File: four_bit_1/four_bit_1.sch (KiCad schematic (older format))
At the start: 1 part, among them P1 DIN_41612_128P

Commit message: Added erasable memory, and fixed lots of random wiring errors.
I decided to go with a 16-bit-wide MRAM chip -- I had  no idea
until I started researching RAM options how technologically
similar MRAM is to core memory. The datasheet diagrams look like
they're straight out of the AGC documentation!

There's a slight inaccuracy in this implementation worth mentioning.
Like fixed memory, I've wired the sense amplifier outputs directly up
to the tristate data output pins of the MRAM chip. But because the
data lines are bidirectional, data being written into RAM will show up
on the sense lines, and go straight into the ungated G register. Since
G is what's being written out, this doesn't matter 99% of the time, but
if there's an overflow condition in G (I don't even know if this is
possible), the bit 16 will be copied over bit 16, and the overflow
condition will be lost. I'll keep an eye out to see if anything relies
on G not changing after the write cycle is complete.

With erasable memory introduced, the computer now theoretically supports
all programs that don't use I/O or interrupts. I've started running
the VirtualAGC validation program, and have been fixing random errors
uncovered by failing self-tests.
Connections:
- net GND: no longer P1.93 (29C), P1.94 (30C), P1.95 (31C), P1.96 (32C)
- new net GEM01: P1.93 (29C)
- new net GEM02: P1.94 (30C)
- new net GEM03: P1.95 (31C)
- new net GEM04: P1.96 (32C)
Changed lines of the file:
@@
 Wire Wire Line
 	4300 8350 4200 8350
-$Comp
-L GND #PWR08
-U 1 1 56A4BF3C
-P 9850 4200
-F 0 "#PWR08" H 9850 3950 50  0001 C CNN
-F 1 "GND" H 9850 4050 50  0000 C CNN
-F 2 "" H 9850 4200 60  0000 C CNN
-F 3 "" H 9850 4200 60  0000 C CNN
-	1    9850 4200
-	1    0    0    -1
-$EndComp
-Wire Wire Line
-	9850 3750 9950 3750
-Wire Wire Line
-	9850 3850 9950 3850
-Connection ~ 9850 3850
-Wire Wire Line
-	9850 3950 9950 3950
-Connection ~ 9850 3950
-Wire Wire Line
-	9850 4050 9950 4050
-Connection ~ 9850 4050
 Wire Wire Line
 	5700 2000 6550 2000
@@
 Wire Wire Line
 	5700 3950 5800 3950
-Wire Wire Line
-	9850 3750 9850 4200
 Text GLabel 9850 2150 0    60   BiDi ~ 0
 RL01/
@@
 Wire Wire Line
 	9950 2450 9850 2450
+Text GLabel 3250 3600 2    60   Output ~ 0
+GEM01
+Wire Wire Line
+	3150 3600 3250 3600
+Text GLabel 3250 3700 2    60   Output ~ 0
+GEM02
+Wire Wire Line
+	3150 3700 3250 3700
+Text GLabel 5800 3600 2    60   Output ~ 0
+GEM03
+Wire Wire Line
+	5700 3600 5800 3600
+Text GLabel 5800 3700 2    60   Output ~ 0
+GEM04
+Wire Wire Line
+	5700 3700 5800 3700
+Text GLabel 9850 3750 0    60   Input ~ 0
+GEM01
+Wire Wire Line
+	9950 3750 9850 3750
+Text GLabel 9850 3850 0    60   Input ~ 0
+GEM02
+Wire Wire Line
+	9950 3850 9850 3850
+Text GLabel 9850 3950 0    60   Input ~ 0
+GEM03
+Wire Wire Line
+	9950 3950 9850 3950
+Text GLabel 9850 4050 0    60   Input ~ 0
+GEM04
+Wire Wire Line
+	9950 4050 9850 4050
 $EndSCHEMATC

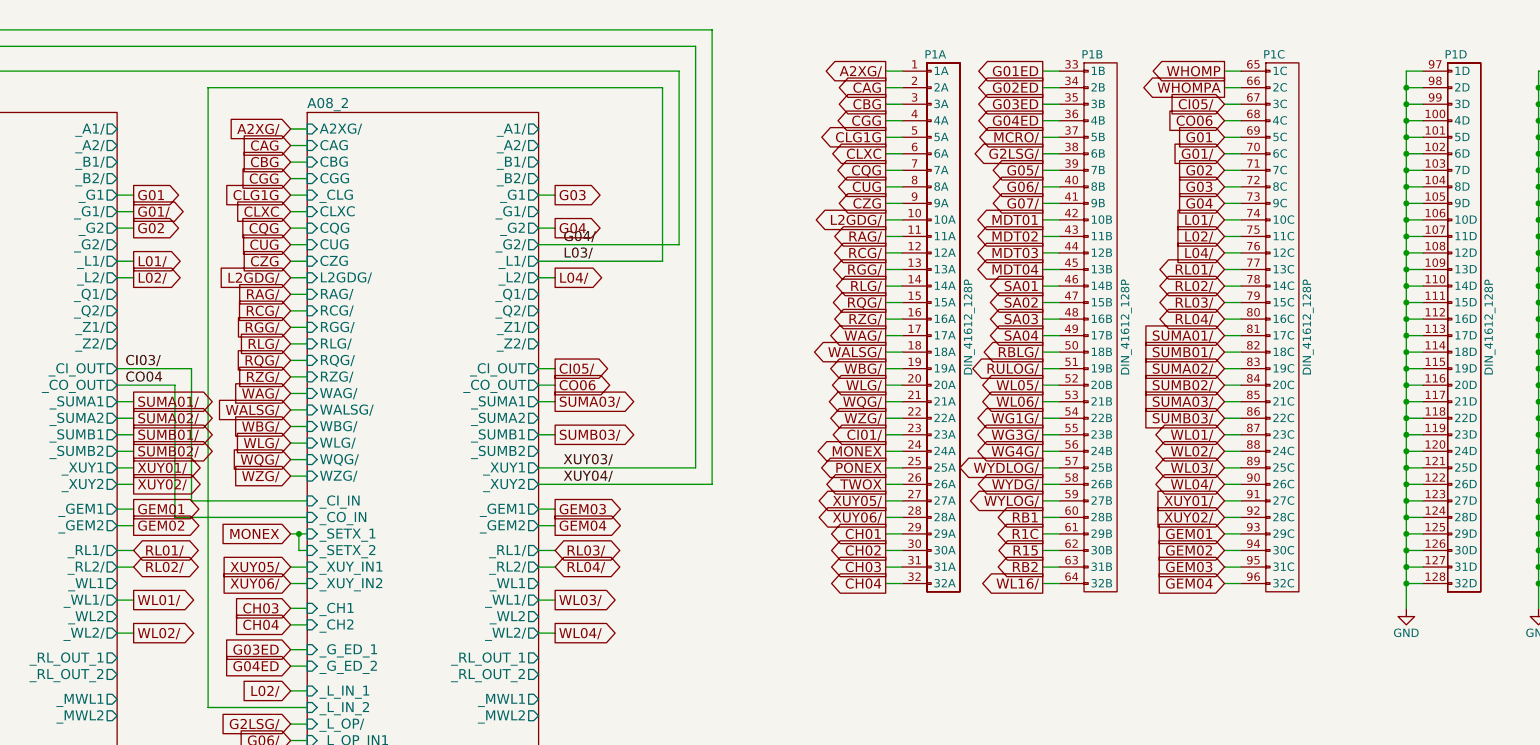
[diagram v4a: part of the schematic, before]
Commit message: Added and tied in Inout VII, the final logic module!
I still need to comb through the schematics to see if there are any
stray gates I missed. The initial conditions are also pretty much
guaranteed to be wrong. But it's mostly all there!
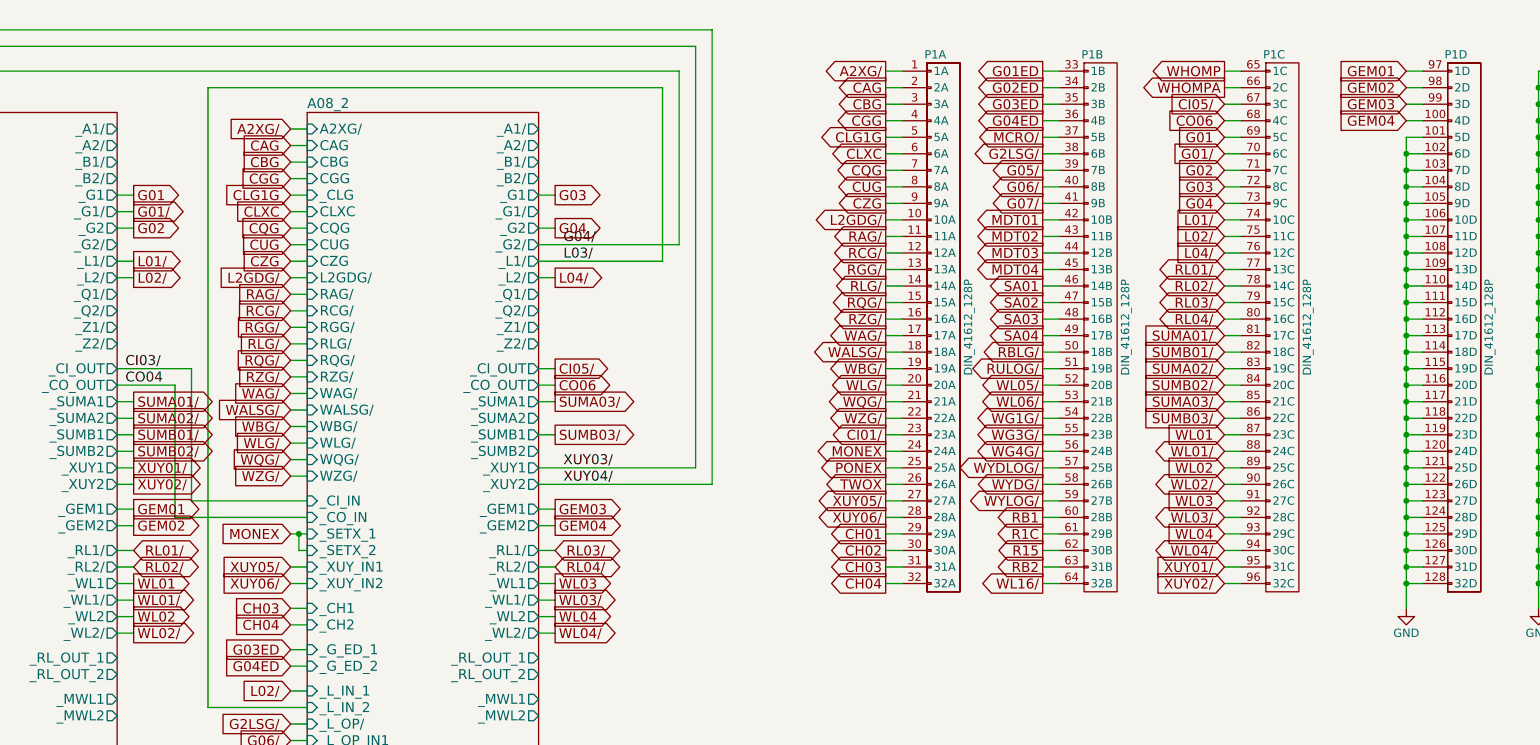
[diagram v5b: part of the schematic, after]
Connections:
- net GEM01: now also P1.97 (1D); no longer P1.93 (29C)
- net GEM02: now also P1.98 (2D); no longer P1.94 (30C)
- net GEM03: now also P1.99 (3D); no longer P1.95 (31C)
- net GEM04: now also P1.100 (4D); no longer P1.96 (32C)
- net GND: no longer P1.100 (4D), P1.97 (1D), P1.98 (2D), P1.99 (3D)
- net WL01/: now also P1.88 (24C); no longer P1.87 (23C)
- net WL02/: now also P1.90 (26C); no longer P1.88 (24C)
- net WL03/: now also P1.92 (28C); no longer P1.89 (25C)
- net WL04/: now also P1.94 (30C); no longer P1.90 (26C)
- net XUY01/: now also P1.95 (31C); no longer P1.91 (27C)
- net XUY02/: now also P1.96 (32C); no longer P1.92 (28C)
- new net WL01: P1.87 (23C)
- new net WL02: P1.89 (25C)
- new net WL03: P1.91 (27C)
- new net WL04: P1.93 (29C)
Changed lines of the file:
@@
 L02/
 Wire Wire Line
-	11050 950  10950 950
-Wire Wire Line
-	11050 1050 10950 1050
-Connection ~ 10950 1050
-Wire Wire Line
-	10950 1150 11050 1150
-Connection ~ 10950 1150
-Wire Wire Line
-	10950 1250 11050 1250
-Connection ~ 10950 1250
-Wire Wire Line
 	10950 1350 11050 1350
-Connection ~ 10950 1350
 Wire Wire Line
 	10950 1450 11050 1450
@@
 	10950 4050 11050 4050
 Connection ~ 10950 4050
-Wire Wire Line
-	10950 950  10950 4200
 Wire Wire Line
 	11850 950  11750 950
@@
 Wire Wire Line
 	9950 1950 9850 1950
-Text GLabel 9850 3150 0    60   BiDi ~ 0
+Text GLabel 9850 3250 0    60   BiDi ~ 0
 WL01/
 Wire Wire Line
-	9950 3150 9850 3150
-Text GLabel 9850 3250 0    60   BiDi ~ 0
+	9950 3250 9850 3250
+Text GLabel 9850 3450 0    60   BiDi ~ 0
 WL02/
 Wire Wire Line
-	9950 3250 9850 3250
-Text GLabel 9850 3350 0    60   BiDi ~ 0
+	9950 3450 9850 3450
+Text GLabel 9850 3650 0    60   BiDi ~ 0
 WL03/
 Wire Wire Line
-	9950 3350 9850 3350
-Text GLabel 9850 3450 0    60   BiDi ~ 0
+	9950 3650 9850 3650
+Text GLabel 9850 3850 0    60   BiDi ~ 0
 WL04/
 Wire Wire Line
-	9950 3450 9850 3450
+	9950 3850 9850 3850
 Text GLabel 5800 2750 2    60   Output ~ 0
 CI05/
@@
 Wire Wire Line
 	3150 3450 3250 3450
-Text GLabel 9850 3550 0    60   Input ~ 0
+Text GLabel 9850 3950 0    60   Input ~ 0
 XUY01/
 Wire Wire Line
-	9950 3550 9850 3550
-Text GLabel 9850 3650 0    60   Input ~ 0
+	9950 3950 9850 3950
+Text GLabel 9850 4050 0    60   Input ~ 0
 XUY02/
 Wire Wire Line
-	9950 3650 9850 3650
+	9950 4050 9850 4050
 Text GLabel 1650 8700 0    60   Input ~ 0
 WHOMPA
@@
 Wire Wire Line
 	5700 3700 5800 3700
+Text GLabel 10950 950  0    60   Input ~ 0
+GEM01
+Wire Wire Line
+	11050 950  10950 950
+Text GLabel 10950 1050 0    60   Input ~ 0
+GEM02
+Wire Wire Line
+	11050 1050 10950 1050
+Text GLabel 10950 1150 0    60   Input ~ 0
+GEM03
+Wire Wire Line
+	11050 1150 10950 1150
+Text GLabel 10950 1250 0    60   Input ~ 0
+GEM04
+Wire Wire Line
+	11050 1250 10950 1250
+Text GLabel 3250 4050 2    60   Output ~ 0
+WL01
+Wire Wire Line
+	3150 4050 3250 4050
+Text GLabel 3250 4250 2    60   Output ~ 0
+WL02
+Wire Wire Line
+	3150 4250 3250 4250
+Text GLabel 5800 4050 2    60   Output ~ 0
+WL03
+Wire Wire Line
+	5700 4050 5800 4050
+Text GLabel 5800 4250 2    60   Output ~ 0
+WL04
+Wire Wire Line
+	5700 4250 5800 4250
+Wire Wire Line
+	10950 1350 10950 4200
+Text GLabel 9850 3150 0    60   Input ~ 0
+WL01
+Wire Wire Line
+	9950 3150 9850 3150
+Text GLabel 9850 3350 0    60   Input ~ 0
+WL02
+Wire Wire Line
+	9950 3350 9850 3350
+Text GLabel 9850 3550 0    60   Input ~ 0
+WL03
+Wire Wire Line
+	9950 3550 9850 3550
 Text GLabel 9850 3750 0    60   Input ~ 0
-GEM01
+WL04
 Wire Wire Line
 	9950 3750 9850 3750
-Text GLabel 9850 3850 0    60   Input ~ 0
-GEM02
-Wire Wire Line
-	9950 3850 9850 3850
-Text GLabel 9850 3950 0    60   Input ~ 0
-GEM03
-Wire Wire Line
-	9950 3950 9850 3950
-Text GLabel 9850 4050 0    60   Input ~ 0
-GEM04
-Wire Wire Line
-	9950 4050 9850 4050
 $EndSCHEMATC

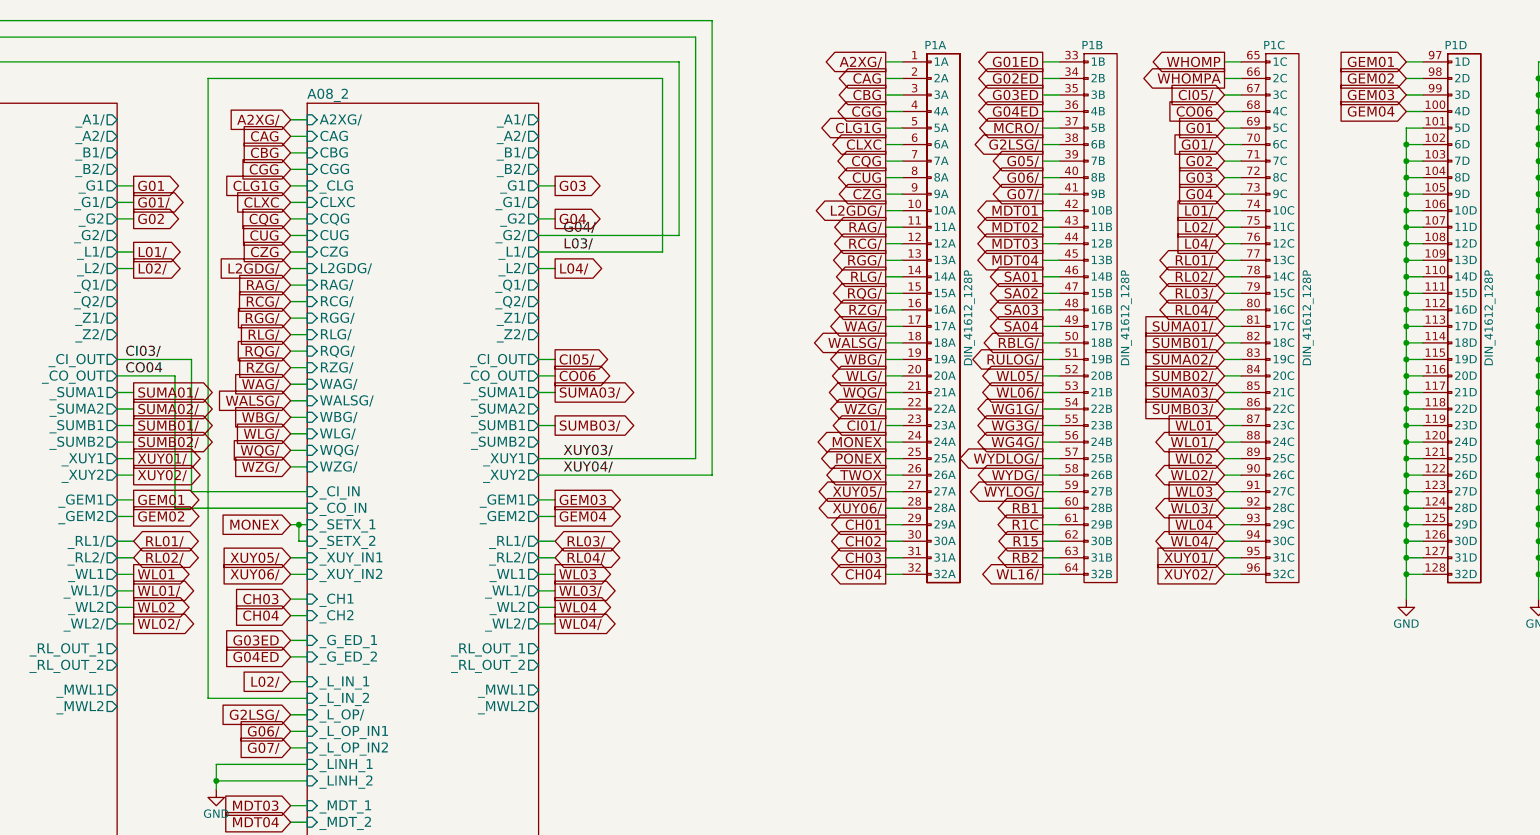
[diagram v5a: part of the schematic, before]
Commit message: Broke all the monitor outputs I could find out to the backplane, in preparation for making a monitor
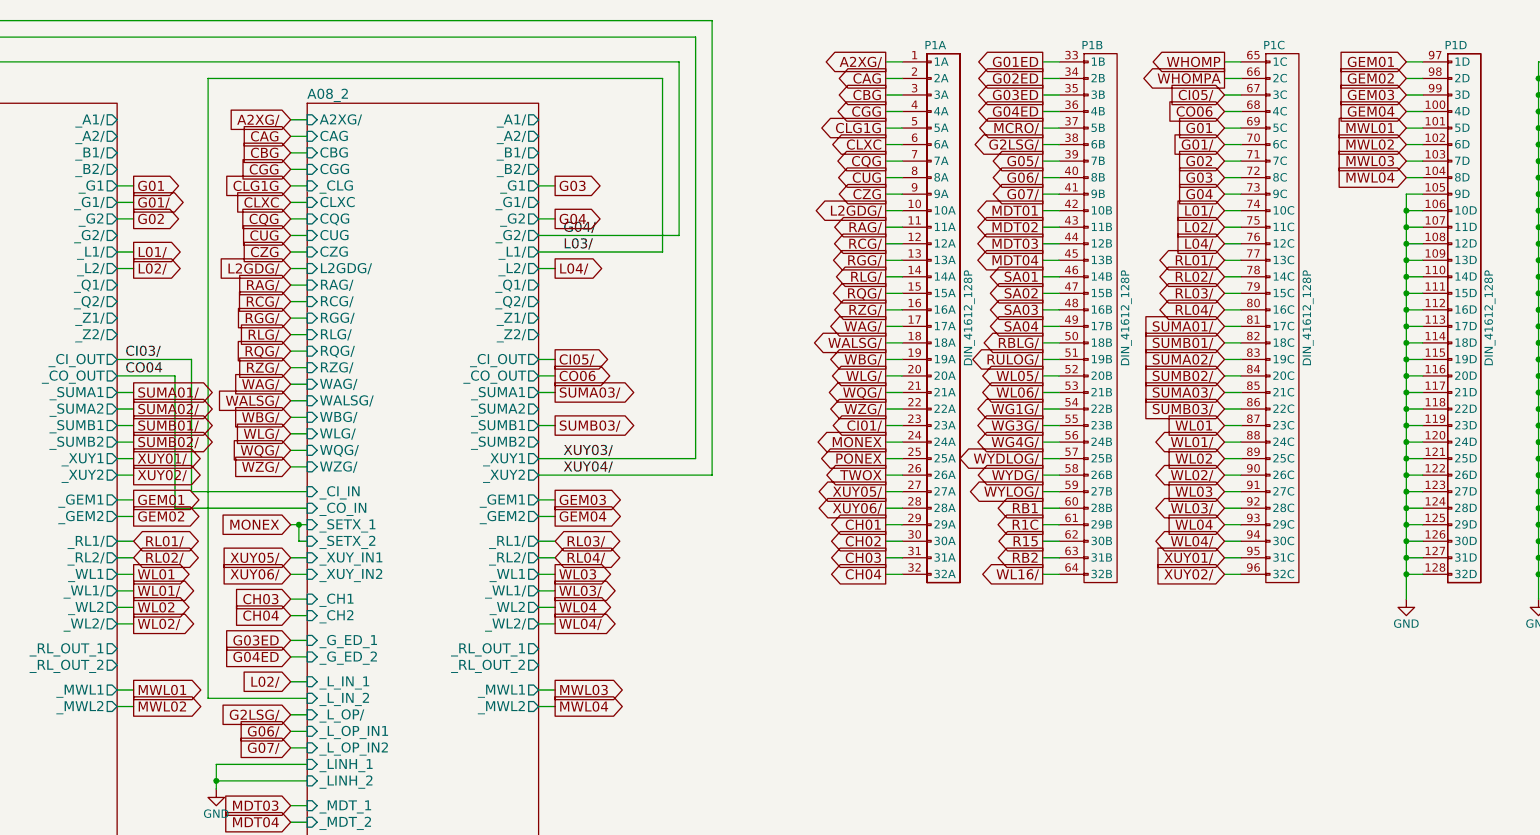
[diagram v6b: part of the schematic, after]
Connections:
- net GND: no longer P1.101 (5D), P1.102 (6D), P1.103 (7D), P1.104 (8D)
- new net MWL01: P1.101 (5D)
- new net MWL02: P1.102 (6D)
- new net MWL03: P1.103 (7D)
- new net MWL04: P1.104 (8D)
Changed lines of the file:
@@
 L02/
 Wire Wire Line
-	10950 1350 11050 1350
-Wire Wire Line
-	10950 1450 11050 1450
-Connection ~ 10950 1450
-Wire Wire Line
-	10950 1550 11050 1550
-Connection ~ 10950 1550
-Wire Wire Line
-	10950 1650 11050 1650
-Connection ~ 10950 1650
-Wire Wire Line
 	10950 1750 11050 1750
-Connection ~ 10950 1750
 Wire Wire Line
 	10950 1850 11050 1850
@@
 Wire Wire Line
 	5700 4250 5800 4250
-Wire Wire Line
-	10950 1350 10950 4200
 Text GLabel 9850 3150 0    60   Input ~ 0
 WL01
@@
 Wire Wire Line
 	9950 3750 9850 3750
+Text GLabel 3250 4850 2    60   Output ~ 0
+MWL02
+Wire Wire Line
+	3150 4850 3250 4850
+Text GLabel 3250 4750 2    60   Output ~ 0
+MWL01
+Wire Wire Line
+	3150 4750 3250 4750
+Text GLabel 5800 4850 2    60   Output ~ 0
+MWL04
+Wire Wire Line
+	5700 4850 5800 4850
+Text GLabel 5800 4750 2    60   Output ~ 0
+MWL03
+Wire Wire Line
+	5700 4750 5800 4750
+Text GLabel 10950 1450 0    60   Input ~ 0
+MWL02
+Wire Wire Line
+	11050 1450 10950 1450
+Text GLabel 10950 1350 0    60   Input ~ 0
+MWL01
+Wire Wire Line
+	11050 1350 10950 1350
+Text GLabel 10950 1650 0    60   Input ~ 0
+MWL04
+Wire Wire Line
+	11050 1650 10950 1650
+Text GLabel 10950 1550 0    60   Input ~ 0
+MWL03
+Wire Wire Line
+	11050 1550 10950 1550
+Wire Wire Line
+	10950 1750 10950 4200
 $EndSCHEMATC
